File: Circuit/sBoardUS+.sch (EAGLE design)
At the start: 37 parts, among them IC1 PIC18F2580-E/SO, IC2 74AC32D, IC3 MAX481CSA, IC4 MC1525TT

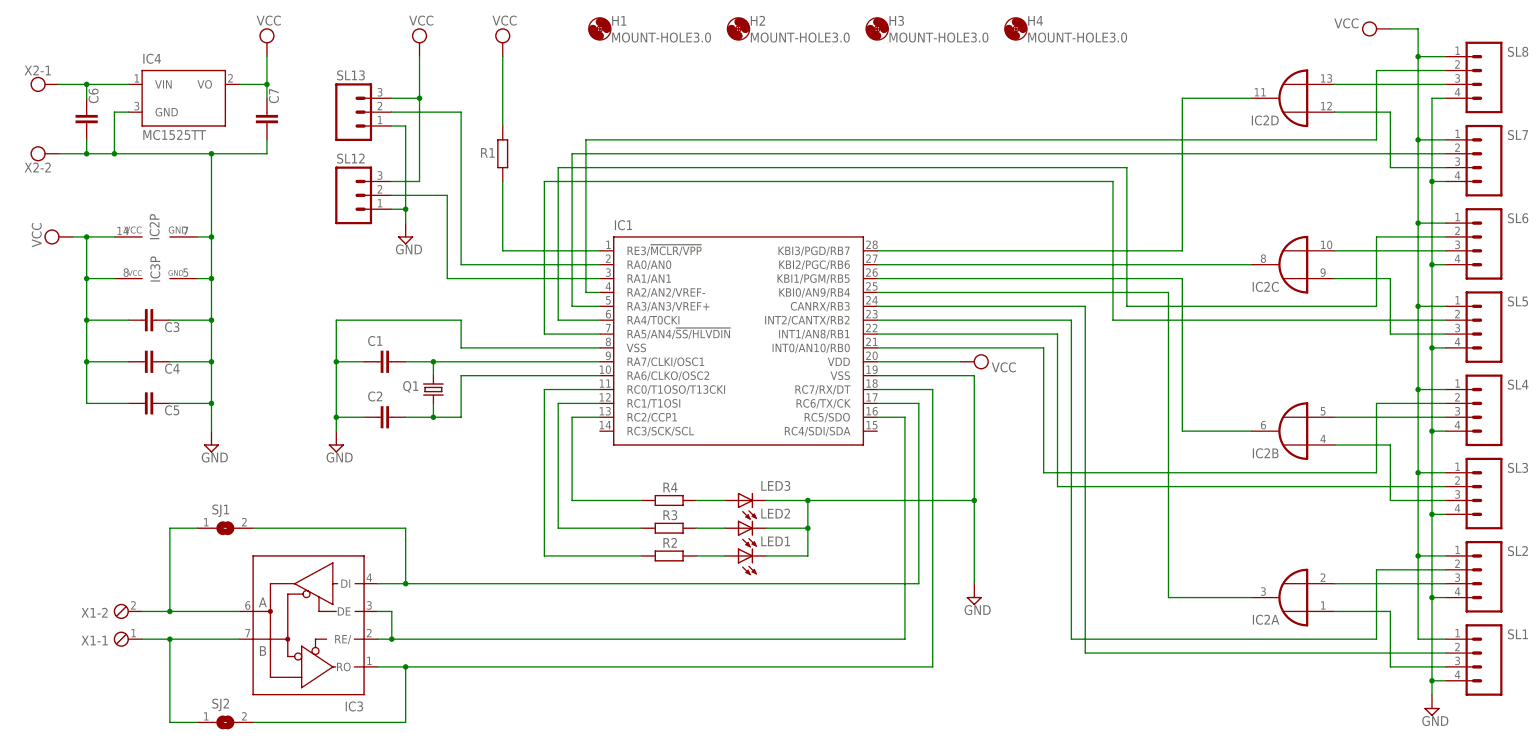
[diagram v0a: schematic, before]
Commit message: Aggiunti i pad per la programmazione ICSP
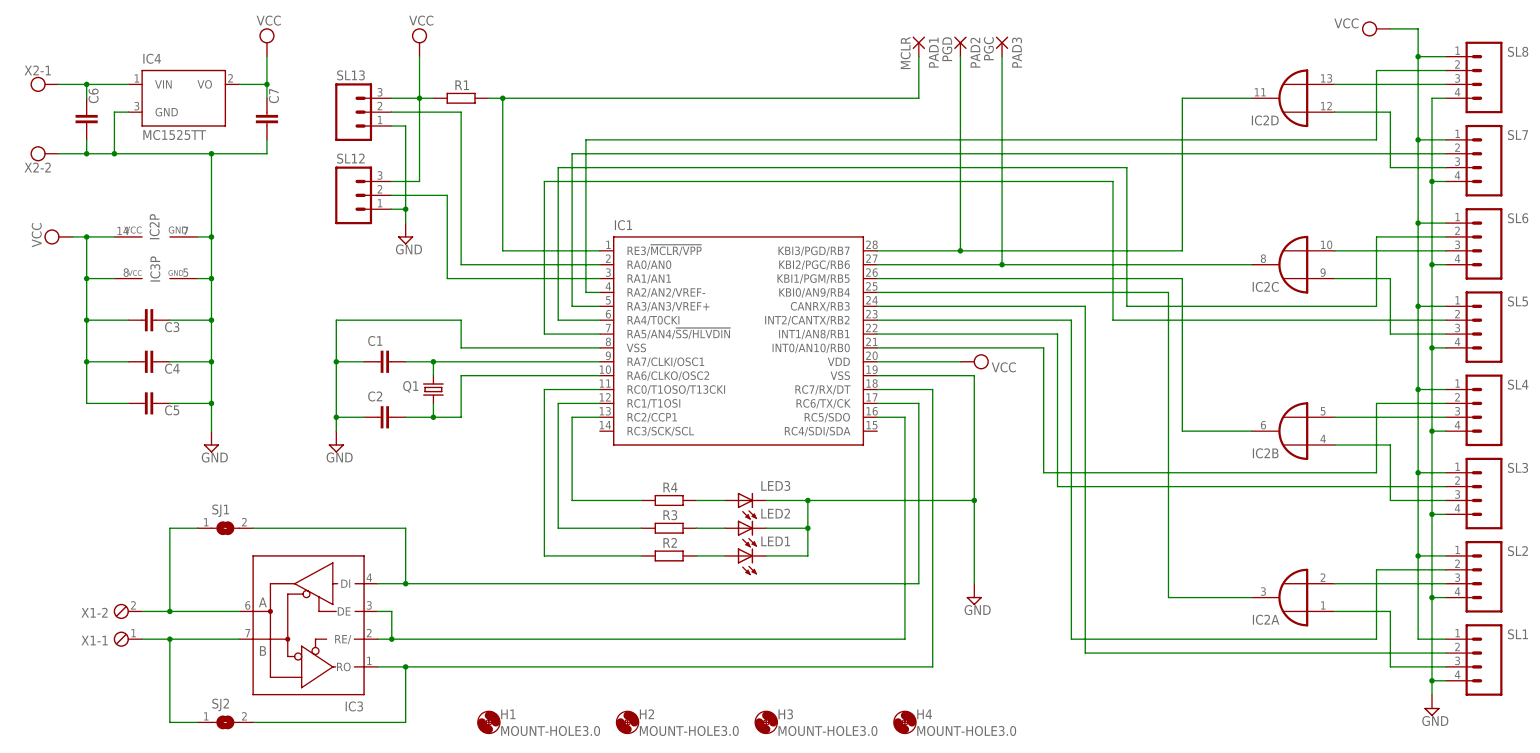
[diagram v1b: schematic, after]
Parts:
- added PAD1: MCLR, wirepad:SMD2
- added PAD2: PGD, wirepad:SMD2
- added PAD3: PGC, wirepad:SMD2
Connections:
- net N$10: now also PAD2.P
- net N$4: now also PAD1.P
- net N$9: now also PAD3.P
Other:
- moved on the sheet: H1, H2, H3, H4, R1
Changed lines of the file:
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@@
 <setting verticaltext="up"/>
 </settings>
-<grid distance="0.1" unitdist="inch" unit="inch" style="dots" multiple="1" display="yes" altdistance="0.01" altunitdist="inch" altunit="inch"/>
+<grid distance="0.1" unitdist="inch" unit="inch" style="lines" multiple="1" display="no" altdistance="0.01" altunitdist="inch" altunit="inch"/>
 <layers>
 <layer number="1" name="Top" color="4" fill="1" visible="no" active="no"/>
@@
 <part name="SL12" library="con-amp-quick" deviceset="M03" device=""/>
 <part name="SL13" library="con-amp-quick" deviceset="M03" device=""/>
-<part name="SUPPLY1" library="supply2" deviceset="VCC" device=""/>
 <part name="SUPPLY2" library="supply2" deviceset="GND" device=""/>
 <part name="IC2" library="74xx-eu" deviceset="74*32" device="D" technology="AC" value=""/>
@@
 <part name="C7" library="rcl" deviceset="C-EU" device="C0805"/>
 <part name="SUPPLY11" library="supply2" deviceset="VCC" device=""/>
+<part name="PAD1" library="wirepad" deviceset="SMD2" device="" value="MCLR"/>
+<part name="PAD2" library="wirepad" deviceset="SMD2" device="" value="PGD"/>
+<part name="PAD3" library="wirepad" deviceset="SMD2" device="" value="PGC"/>
 </parts>
 <sheets>
@@
 <attribute name="VALUE" x="25.019" y="34.544" size="1.778" layer="96" rot="R90"/>
 </instance>
-<instance part="R1" gate="G$1" x="43.18" y="81.28" smashed="yes" rot="R90">
-<attribute name="NAME" x="41.91" y="82.3214" size="1.778" layer="95" rot="R180"/>
-<attribute name="VALUE" x="46.482" y="77.47" size="1.778" layer="96" rot="R90"/>
+<instance part="R1" gate="G$1" x="35.56" y="91.44" smashed="yes" rot="R180">
+<attribute name="NAME" x="34.29" y="92.9386" size="1.778" layer="95"/>
+<attribute name="VALUE" x="39.37" y="94.742" size="1.778" layer="96" rot="R180"/>
 </instance>
 <instance part="SL12" gate="G$1" x="15.24" y="73.66"/>
 <instance part="SL13" gate="G$1" x="15.24" y="88.9"/>
-<instance part="SUPPLY1" gate="G$1" x="43.18" y="101.6"/>
 <instance part="SUPPLY2" gate="GND" x="12.7" y="27.94"/>
 <instance part="IC2" gate="A" x="187.96" y="0" rot="R180"/>
@@
 <attribute name="VALUE" x="77.47" y="21.082" size="1.778" layer="96" rot="R180"/>
 </instance>
-<instance part="H1" gate="G$1" x="60.96" y="104.14"/>
-<instance part="H2" gate="G$1" x="86.36" y="104.14"/>
-<instance part="H3" gate="G$1" x="111.76" y="104.14"/>
-<instance part="H4" gate="G$1" x="137.16" y="104.14"/>
+<instance part="H1" gate="G$1" x="40.64" y="-22.86"/>
+<instance part="H2" gate="G$1" x="66.04" y="-22.86"/>
+<instance part="H3" gate="G$1" x="91.44" y="-22.86"/>
+<instance part="H4" gate="G$1" x="116.84" y="-22.86"/>
 <instance part="IC4" gate="G$1" x="-15.24" y="91.44"/>
 <instance part="C6" gate="G$1" x="-33.02" y="88.9" smashed="yes">
@@
 </instance>
 <instance part="SUPPLY11" gate="G$1" x="0" y="101.6"/>
+<instance part="PAD1" gate="1" x="119.38" y="101.6" rot="R270"/>
+<instance part="PAD2" gate="1" x="127" y="101.6" rot="R270"/>
+<instance part="PAD3" gate="1" x="134.62" y="101.6" rot="R270"/>
 </instances>
 <busses>
@@
 <net name="VCC" class="0">
 <segment>
-<pinref part="SUPPLY1" gate="G$1" pin="VCC"/>
-<pinref part="R1" gate="G$1" pin="2"/>
-<wire x1="43.18" y1="99.06" x2="43.18" y2="86.36" width="0.1524" layer="91"/>
-</segment>
-<segment>
 <pinref part="SL12" gate="G$1" pin="3"/>
 <pinref part="SUPPLY4" gate="G$1" pin="VCC"/>
@@
 <wire x1="22.86" y1="91.44" x2="27.94" y2="91.44" width="0.1524" layer="91"/>
 <junction x="27.94" y="91.44"/>
+<pinref part="R1" gate="G$1" pin="2"/>
+<wire x1="30.48" y1="91.44" x2="27.94" y2="91.44" width="0.1524" layer="91"/>
 </segment>
 <segment>
@@
 <pinref part="IC2" gate="C" pin="O"/>
 <pinref part="IC1" gate="G$1" pin="KBI2/PGC/RB6"/>
-<wire x1="180.34" y1="60.96" x2="111.76" y2="60.96" width="0.1524" layer="91"/>
+<wire x1="180.34" y1="60.96" x2="134.62" y2="60.96" width="0.1524" layer="91"/>
+<wire x1="134.62" y1="60.96" x2="111.76" y2="60.96" width="0.1524" layer="91"/>
+<wire x1="134.62" y1="99.06" x2="134.62" y2="60.96" width="0.1524" layer="91"/>
+<junction x="134.62" y="60.96"/>
+<pinref part="PAD3" gate="1" pin="P"/>
 </segment>
 </net>
@@
 <segment>
 <pinref part="IC1" gate="G$1" pin="KBI3/PGD/RB7"/>
-<wire x1="111.76" y1="63.5" x2="167.64" y2="63.5" width="0.1524" layer="91"/>
+<wire x1="111.76" y1="63.5" x2="127" y2="63.5" width="0.1524" layer="91"/>
+<wire x1="127" y1="63.5" x2="167.64" y2="63.5" width="0.1524" layer="91"/>
 <wire x1="167.64" y1="63.5" x2="167.64" y2="91.44" width="0.1524" layer="91"/>
 <pinref part="IC2" gate="D" pin="O"/>
 <wire x1="167.64" y1="91.44" x2="180.34" y2="91.44" width="0.1524" layer="91"/>
+<wire x1="127" y1="99.06" x2="127" y2="63.5" width="0.1524" layer="91"/>
+<junction x="127" y="63.5"/>
+<pinref part="PAD2" gate="1" pin="P"/>
 </segment>
 </net>
@@
 <segment>
 <pinref part="IC1" gate="G$1" pin="RE3/!MCLR/VPP"/>
+<wire x1="60.96" y1="63.5" x2="43.18" y2="63.5" width="0.1524" layer="91"/>
+<wire x1="43.18" y1="63.5" x2="43.18" y2="91.44" width="0.1524" layer="91"/>
 <pinref part="R1" gate="G$1" pin="1"/>
-<wire x1="60.96" y1="63.5" x2="43.18" y2="63.5" width="0.1524" layer="91"/>
-<wire x1="43.18" y1="63.5" x2="43.18" y2="76.2" width="0.1524" layer="91"/>
-</segment>
-</net>
+<wire x1="43.18" y1="91.44" x2="40.64" y2="91.44" width="0.1524" layer="91"/>
+<wire x1="43.18" y1="91.44" x2="119.38" y2="91.44" width="0.1524" layer="91"/>
+<wire x1="119.38" y1="91.44" x2="119.38" y2="99.06" width="0.1524" layer="91"/>
+<junction x="43.18" y="91.44"/>
+<pinref part="PAD1" gate="1" pin="P"/>
+</segment>
+</net>
